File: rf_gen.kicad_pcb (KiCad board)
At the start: 2 copper layers, 101.6 x 35.7 mm, 53 parts, among them J1 Conn_01x07_Male, J2 Screw_Terminal_01x04, J3 Conn_01x05_Male, Q1 GS61004B, Q2 G3R350MT12J, U1 NPC81074, U2 AP62150

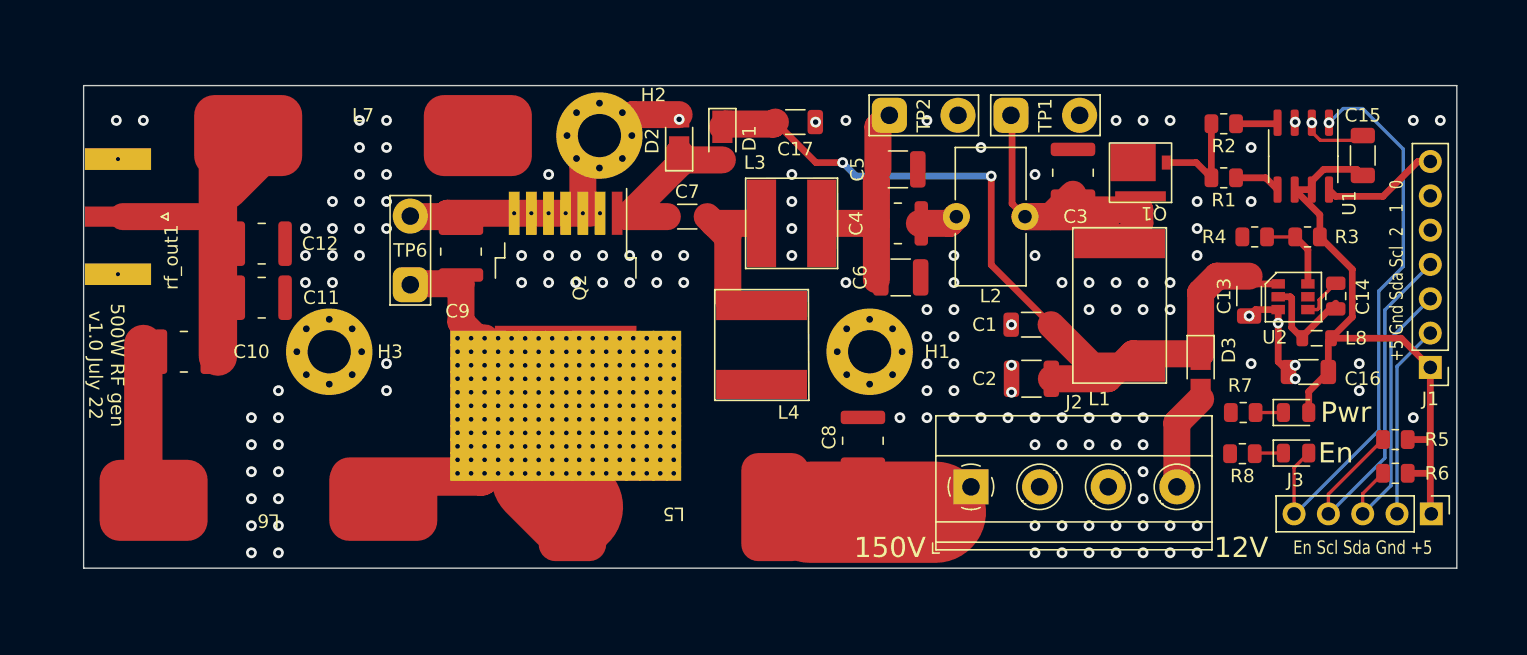
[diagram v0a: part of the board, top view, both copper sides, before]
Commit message: Updated PCB due to inductor changes
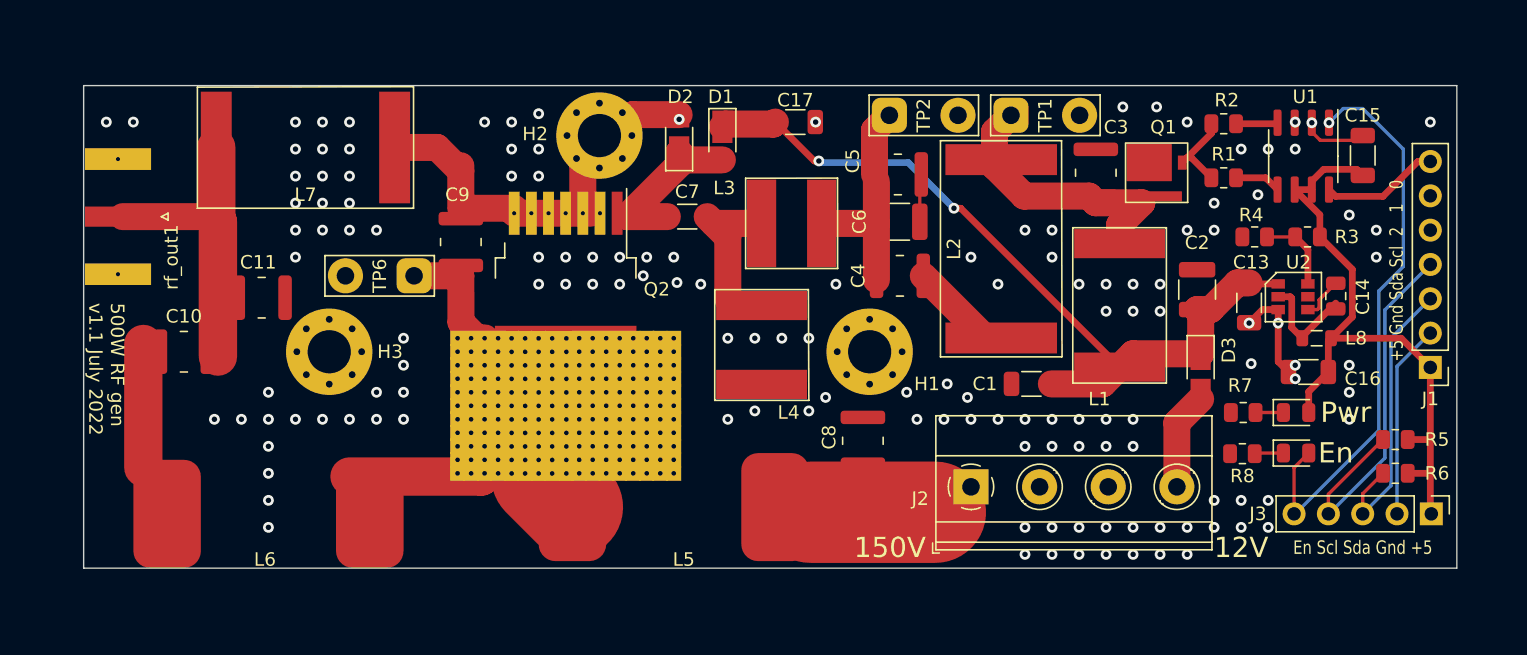
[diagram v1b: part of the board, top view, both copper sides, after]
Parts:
- removed C12: 12p, rf_gen:C_1111_2828Metric
- removed REF**: heatsink_45x45, rf_gen:heatsink_45x45
- C10, C9: value 39p -> 180p
- C11, C8: value 220p -> 270p
- C5: value 470p -> 220p; footprint Capacitor_SMD:C_1210_3225Metric -> rf_gen:C_1111_2828Metric
- L2: value 650n -> 500n; footprint rf_gen:L_Toroid_Vertical_L10.0mm_W5.0mm_P5.08mm -> rf_gen:2929SQ-501
- L6: value 3.5u -> 760n; footprint rf_gen:inductor_core_25x18 -> rf_gen:inductor_air_15x15
- L7: value 594n -> 500n; footprint rf_gen:inductor_core_25x18 -> rf_gen:2929SQ-501
- moved C2 13.9 mm to (151.0, 119.5), turned to -90 degrees
- moved L7 4.66 mm to (85.0, 109.0)
- moved C1 4.38 mm to (138.7, 126.5)
- moved C6 4.12 mm to (129.0, 114.5)
- moved C4 3.88 mm to (129.0, 118.5)
- moved L2 2.96 mm to (136.5, 116.5)
- moved C3 1.69 mm to (143.5, 110.9)
- moved Q1 1.19 mm to (148.0, 110.9)
- moved TP6 0.72 mm to (93.0, 118.5), turned to 180 degrees
- moved C9 0.71 mm to (96.5, 116.0)
- moved C13 0.50 mm to (154.8, 120.5)
- moved C5 0.38 mm to (128.8, 111.0)
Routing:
- net GND: track 50.0 -> 60.1 mm, vias 135 -> 140
- net Net-(C3-Pad2): track 29.9 -> 20.0 mm
- net Net-(C10-Pad2): track 28.7 -> 22.7 mm
- net Net-(C4-Pad1): track 2.95 -> 7.68 mm
- net +12V: track 61.8 -> 58.7 mm
- net /GaN_gate: track 7.81 -> 6.18 mm
- net Net-(C9-Pad2): track 24.3 -> 25.5 mm
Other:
- board text added: "500W RF gen v1.1 July 2022"
- board text removed: "500W RF gen v1.0 July 22"
